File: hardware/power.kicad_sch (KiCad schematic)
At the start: 29 parts, among them J2 batt, Q1 NPN SS8050, SW57 SW_SPDT, U3 BQ24075RGT, U4 TLV62569DBV

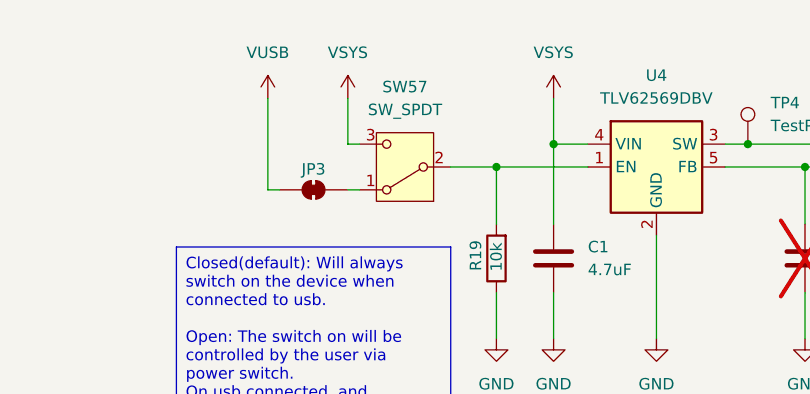
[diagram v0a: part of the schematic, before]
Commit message: set footprints, some lcsc codes
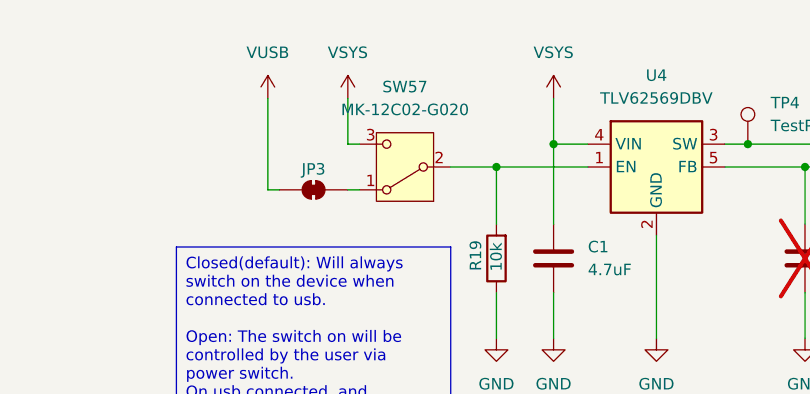
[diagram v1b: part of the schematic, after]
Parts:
- C1, C2, C3, C4, C5: footprint (none) -> Capacitor_SMD:C_0603_1608Metric
- D1: footprint (none) -> LED_SMD:LED_0603_1608Metric
- J2: footprint (none) -> Battery:BatteryHolder_Keystone_1042_1x18650
- L1: footprint (none) -> Inductor_SMD:L_Coilcraft_XxL4040
- R16, R21, R22, R23: footprint (none) -> Resistor_SMD:R_0603_1608Metric
- SW57: value SW_SPDT -> MK-12C02-G020; footprint (none) -> Button_Switch_SMD:SW_SPDT_PCM12; LCSC (none) -> C963206
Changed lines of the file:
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@@
 			)
 		)
-		(property "Value" "SW_SPDT"
+		(property "Value" " MK-12C02-G020"
 			(at 96.52 33.02 0)
 			(effects
@@
 			)
 		)
-		(property "Footprint" ""
+		(property "Footprint" "Button_Switch_SMD:SW_SPDT_PCM12"
 			(at 96.52 39.37 0)
 			(effects
@@
 			)
 		)
+		(property "LCSC" "C963206"
+			(at 96.52 39.37 0)
+			(effects
+				(font
+					(size 1.27 1.27)
+				)
+				(hide yes)
+			)
+		)
 		(pin "2"
 		)
@@
 			)
 		)
-		(property "Footprint" ""
+		(property "Footprint" "LED_SMD:LED_0603_1608Metric"
 			(at 191.77 124.46 0)
 			(effects
@@
 			)
 		)
-		(property "Footprint" ""
+		(property "Footprint" "Resistor_SMD:R_0603_1608Metric"
 			(at 177.292 41.91 90)
 			(effects
@@
 			)
 		)
-		(property "Footprint" ""
+		(property "Footprint" "Capacitor_SMD:C_0603_1608Metric"
 			(at 113.9952 53.34 0)
 			(effects
@@
 			)
 		)
-		(property "Footprint" ""
+		(property "Footprint" "Inductor_SMD:L_Coilcraft_XxL4040"
 			(at 151.13 36.83 0)
 			(effects
@@
 			)
 		)
-		(property "Footprint" ""
+		(property "Footprint" "Capacitor_SMD:C_0603_1608Metric"
 			(at 141.9352 53.34 0)
 			(effects
@@
 			)
 		)
-		(property "Footprint" ""
+		(property "Footprint" "Capacitor_SMD:C_0603_1608Metric"
 			(at 143.2052 143.51 0)
 			(effects
@@
 			)
 		)
-		(property "Footprint" ""
+		(property "Footprint" "Resistor_SMD:R_0603_1608Metric"
 			(at 177.292 54.61 90)
 			(effects
@@
 			)
 		)
-		(property "Footprint" ""
+		(property "Footprint" "Capacitor_SMD:C_0603_1608Metric"
 			(at 162.2552 45.72 0)
 			(effects
@@
 			)
 		)
-		(property "Footprint" ""
+		(property "Footprint" "Battery:BatteryHolder_Keystone_1042_1x18650"
 			(at 160.02 137.16 0)
 			(effects
@@
 			)
 		)
-		(property "Footprint" ""
+		(property "Footprint" "Resistor_SMD:R_0603_1608Metric"
 			(at 64.262 153.67 90)
 			(effects
@@
 			)
 		)
-		(property "Footprint" ""
+		(property "Footprint" "Resistor_SMD:R_0603_1608Metric"
 			(at 193.548 133.35 90)
 			(effects
@@
 			)
 		)
-		(property "Footprint" ""
+		(property "Footprint" "Capacitor_SMD:C_0603_1608Metric"
 			(at 168.6052 147.32 0)
 			(effects

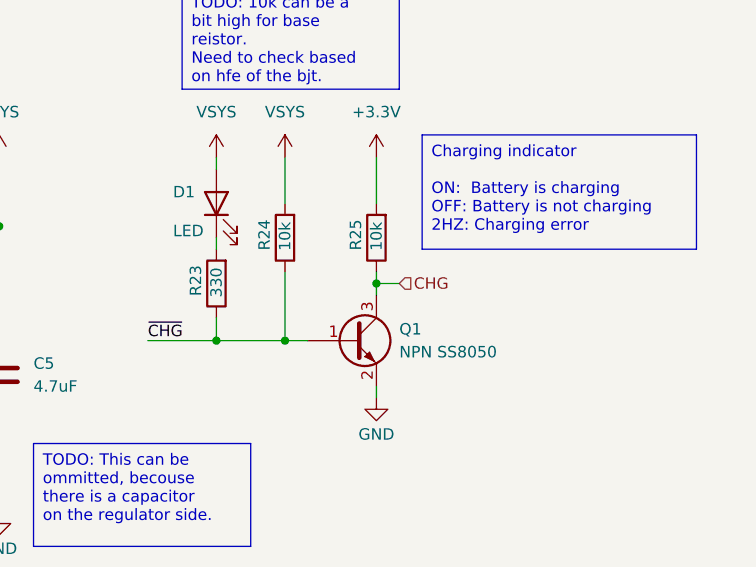
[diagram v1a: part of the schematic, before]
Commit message: lcd wires, wire direction
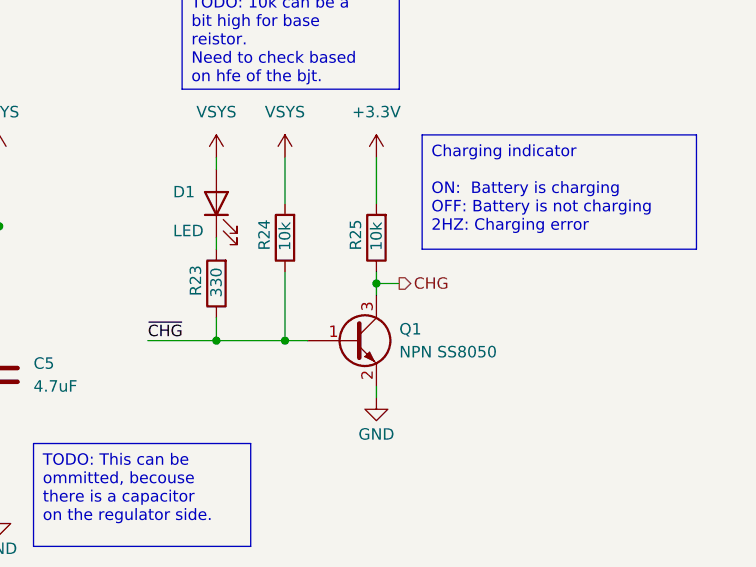
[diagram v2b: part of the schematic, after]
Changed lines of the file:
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@@
 	)
 	(hierarchical_label "CHG"
-		(shape input)
+		(shape output)
 		(at 212.09 133.35 0)
 		(fields_autoplaced yes)

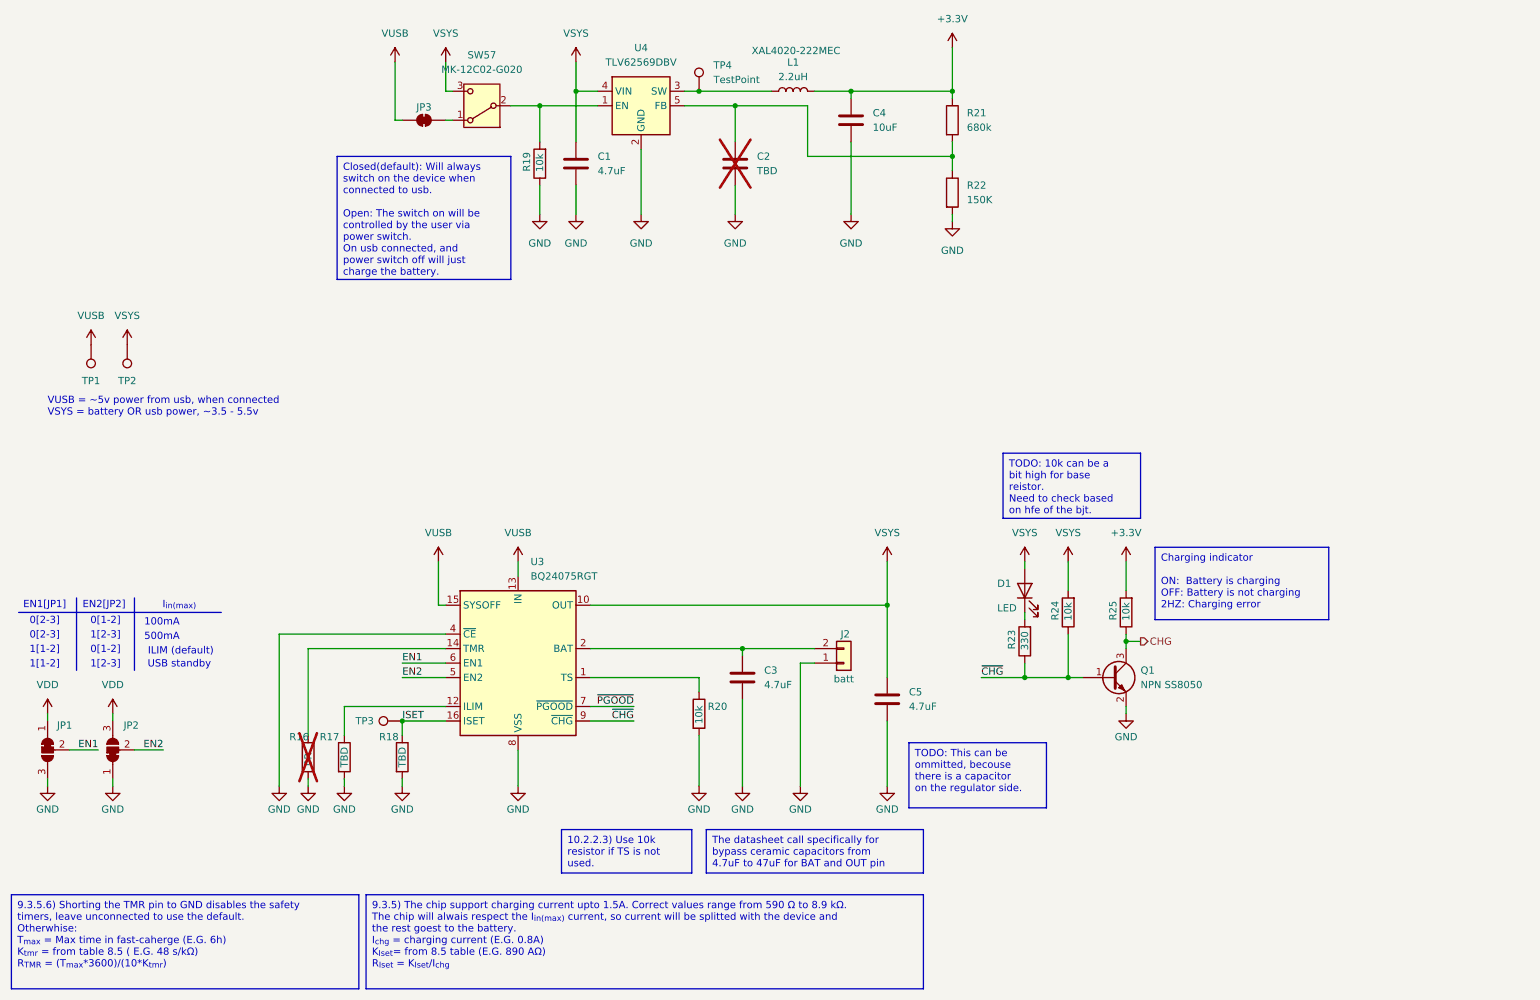
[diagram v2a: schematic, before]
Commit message: battery voltage divider
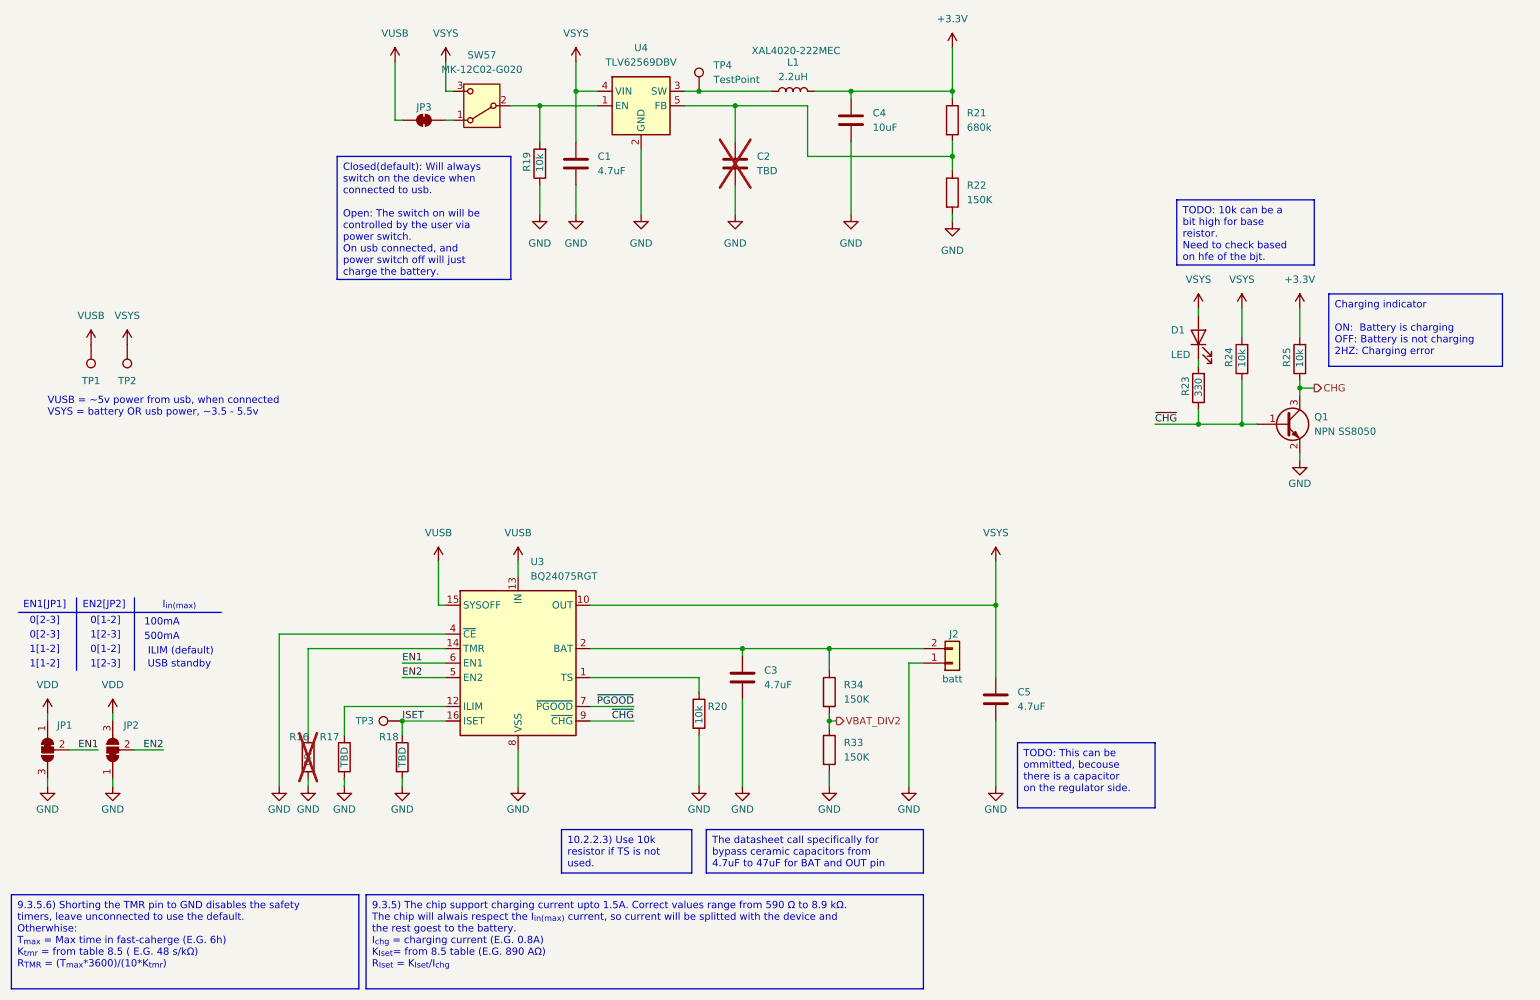
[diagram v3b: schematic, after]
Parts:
- added R33, R34: 150K, Resistor_SMD:R_0603_1608Metric, symbol Device:R
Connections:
- net GND: now also R33.2
- net at C3.1, J2.2 (Pin_2), U3.2 (BAT)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: now also R34.1
- new net VBAT_DIV2: R33.1, R34.2
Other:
- moved on the sheet: C5, D1, J2, Q1, R23, R24, R25

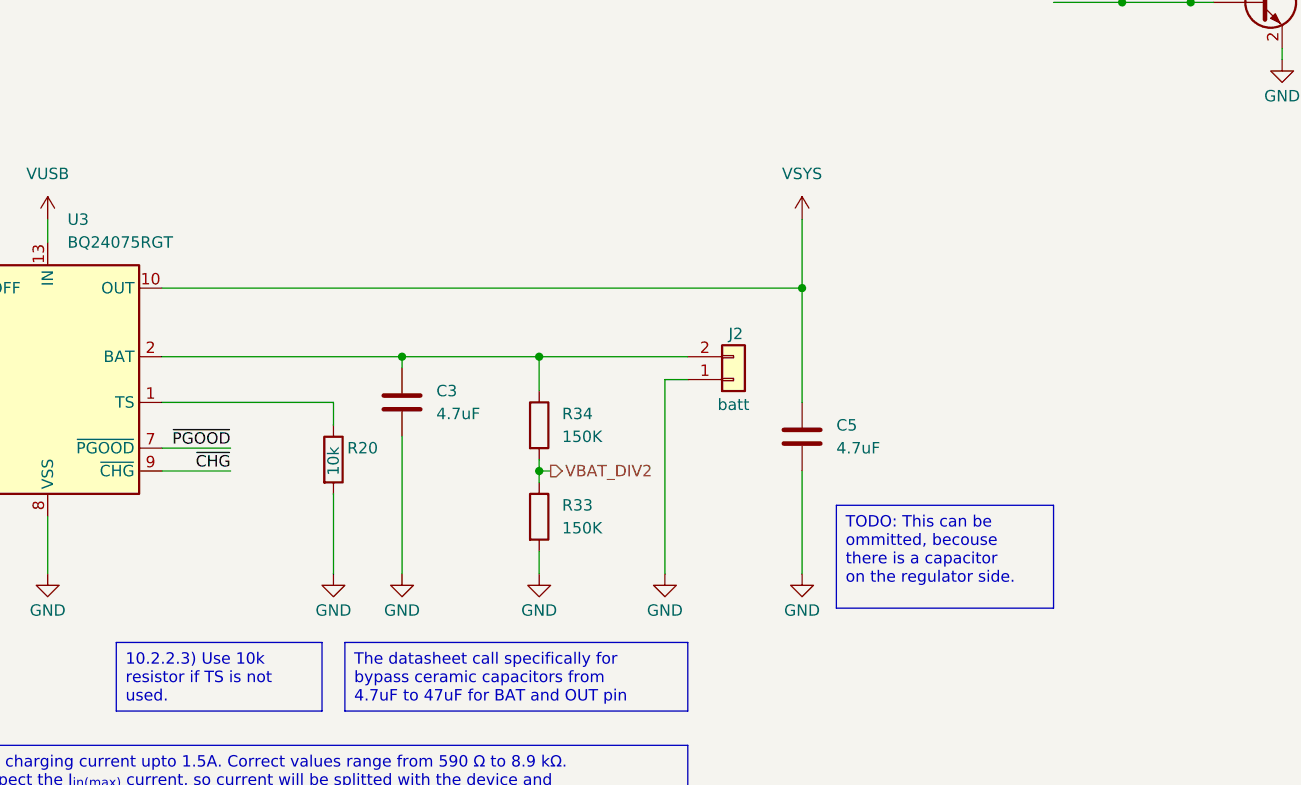
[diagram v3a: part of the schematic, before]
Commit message: move voltage divider from bat to vsys
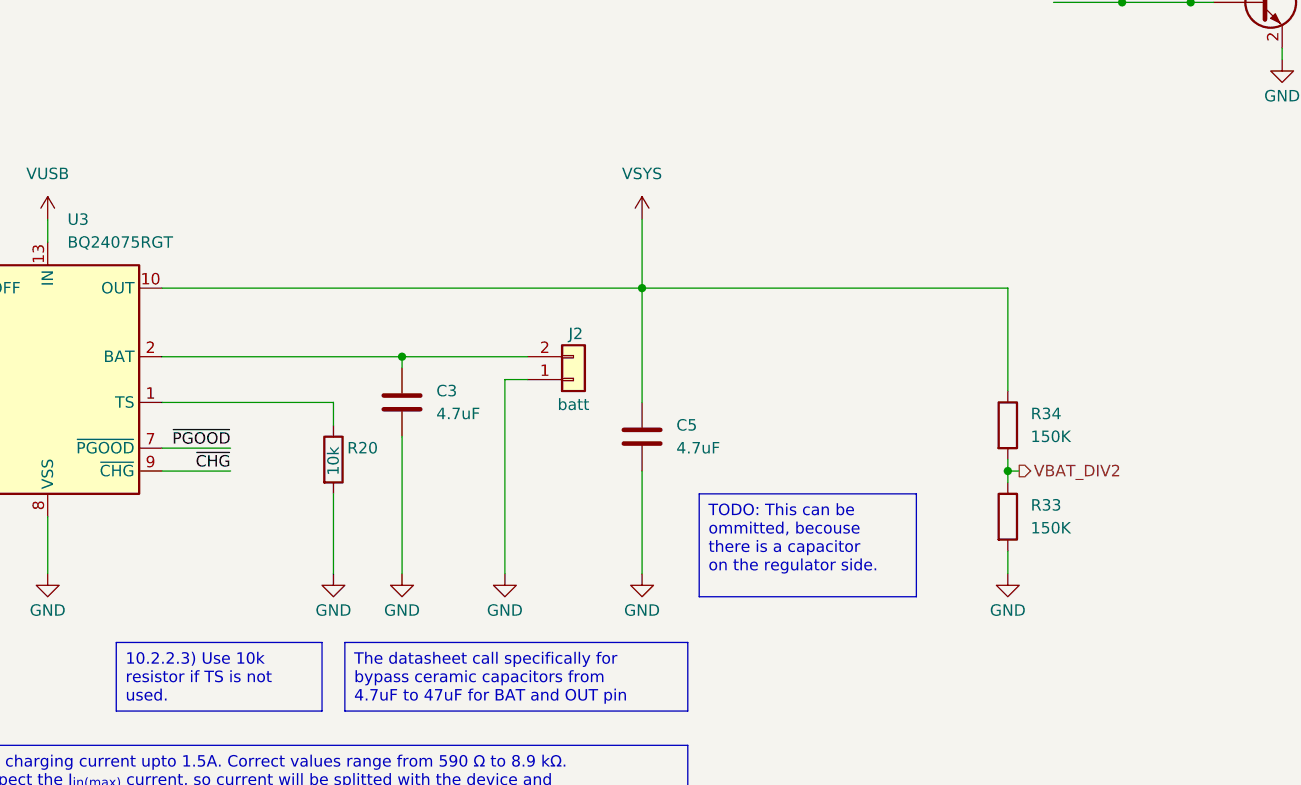
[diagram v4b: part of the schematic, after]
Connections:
- net VSYS: now also R34.1
- net at C3.1, J2.2 (Pin_2), U3.2 (BAT)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: no longer R34.1
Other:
- moved on the sheet: C5, J2, R33, R34

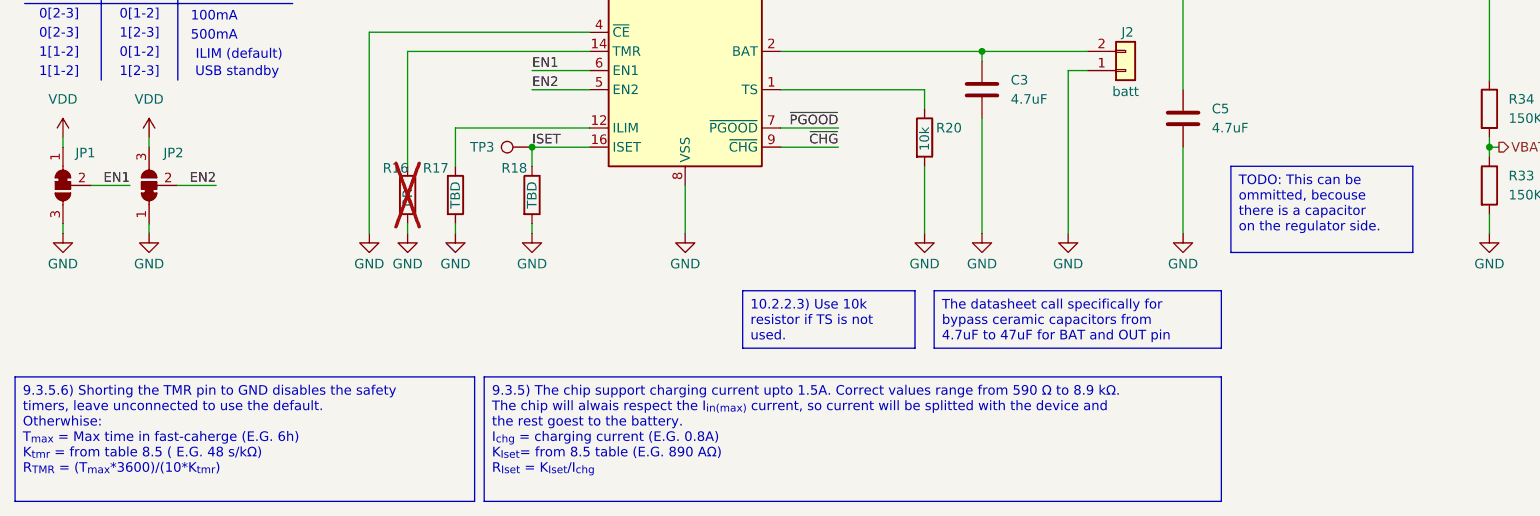
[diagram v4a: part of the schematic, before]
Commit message: Calculate the resistor values for the BMS
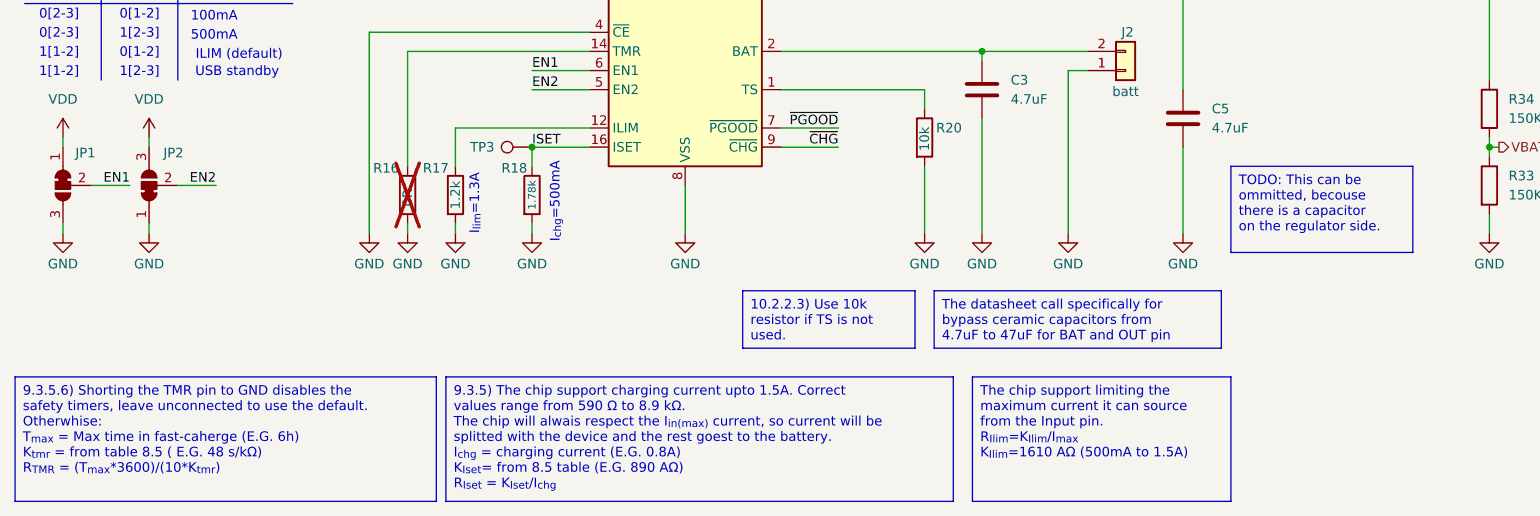
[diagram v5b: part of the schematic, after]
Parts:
- R17: value TBD -> 1.2k
- R18: value TBD -> 1.78k
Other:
- note added: "I_{chg}=500mA"
- note added: "I_{lim}=1.3A"
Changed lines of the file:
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@@
 		(exclude_from_sim no)
 		(at 13.97 177.8 0)
-		(size 60.96 16.51)
+		(size 55.88 16.51)
 		(stroke
 			(width 0)
@@
 		)
 	)
+	(text_box "The chip support limiting the maximum current it can source from the Input pin.\nR_{Ilim}=K_{Ilim}/I_{max}\nK_{Ilim}=1610 AΩ (500mA to 1.5A)"
+		(exclude_from_sim no)
+		(at 140.97 177.8 0)
+		(size 34.29 16.51)
+		(stroke
+			(width 0)
+			(type default)
+		)
+		(fill
+			(type none)
+		)
+		(effects
+			(font
+				(size 1.27 1.27)
+			)
+			(justify left top)
+		)
+	)
 	(text_box "The datasheet call specifically for bypass ceramic capacitors from 4.7uF to 47uF for BAT and OUT pin"
 		(exclude_from_sim no)
@@
 	(text_box "9.3.5) The chip support charging current upto 1.5A. Correct values range from 590 Ω to 8.9 kΩ.\nThe chip will alwais respect the I_{in(max)} current, so current will be splitted with the device and the rest goest to the battery.\nI_{chg} = charging current (E.G. 0.8A)\nK_{Iset}= from 8.5 table (E.G. 890 AΩ)\nR_{Iset} = K_{Iset}/I_{chg}"
 		(exclude_from_sim no)
-		(at 76.2 177.8 0)
-		(size 97.79 16.51)
+		(at 71.12 177.8 0)
+		(size 67.31 16.51)
 		(stroke
 			(width 0)
@@
 		)
 	)
+	(text "I_{chg}=500mA"
+		(exclude_from_sim no)
+		(at 85.598 154.686 90)
+		(effects
+			(font
+				(size 1.27 1.27)
+			)
+		)
+	)
 	(text "EN2[JP2]"
 		(exclude_from_sim no)
@@
 		)
 	)
+	(text "I_{lim}=1.3A"
+		(exclude_from_sim no)
+		(at 74.93 154.94 90)
+		(effects
+			(font
+				(size 1.27 1.27)
+			)
+		)
+	)
 	(text "ILIM (default)"
 		(exclude_from_sim no)
@@
 			)
 		)
-		(property "Value" "TBD"
+		(property "Value" "1.78k"
 			(at 82.55 153.67 90)
 			(effects
 				(font
-					(size 1.27 1.27)
+					(size 1.016 1.016)
 				)
 			)
@@
 			)
 		)
-		(property "Value" "TBD"
+		(property "Value" "1.2k"
 			(at 72.39 153.67 90)
 			(effects
@@
 		(dnp yes)
 		(property "Reference" "R16"
-			(at 62.738 150.114 0)
+			(at 61.468 150.114 0)
 			(effects
 				(font
